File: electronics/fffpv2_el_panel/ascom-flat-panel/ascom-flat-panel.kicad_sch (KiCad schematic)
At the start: 19 parts, among them J1 Servo, J2 Conn_01x02, Q1 IRLZ34N, Q2 IRLZ34N, U1 XIAO-SAMD21-DIP, U2 TLC272

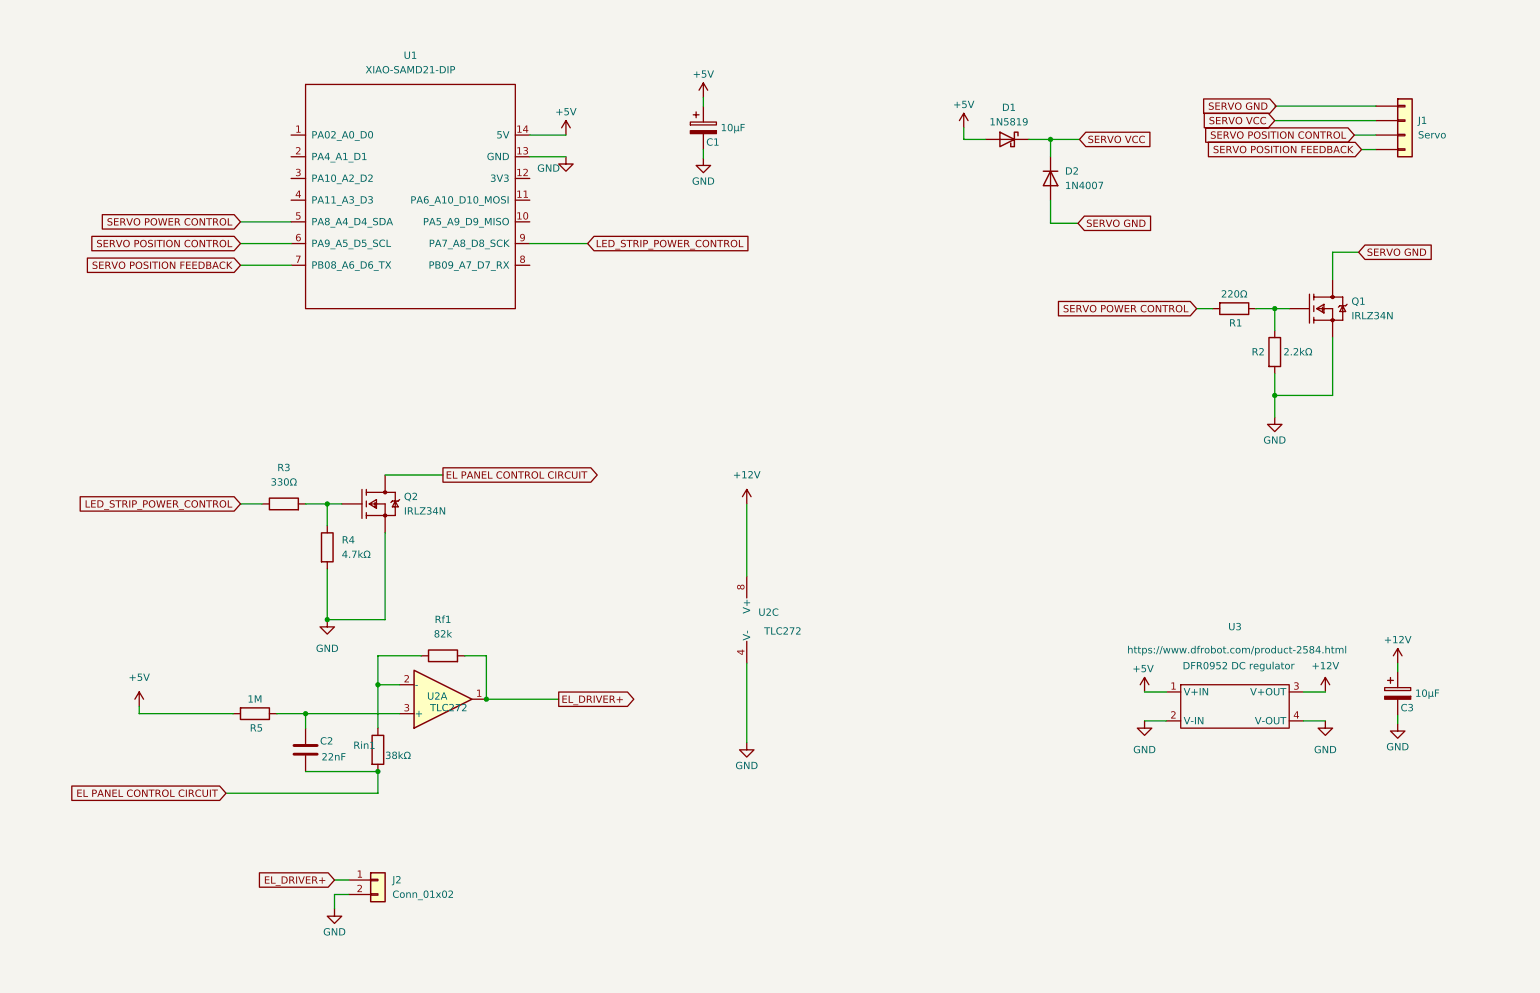
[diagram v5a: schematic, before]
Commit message: Flip connector for shorter traces and rearanged schematics
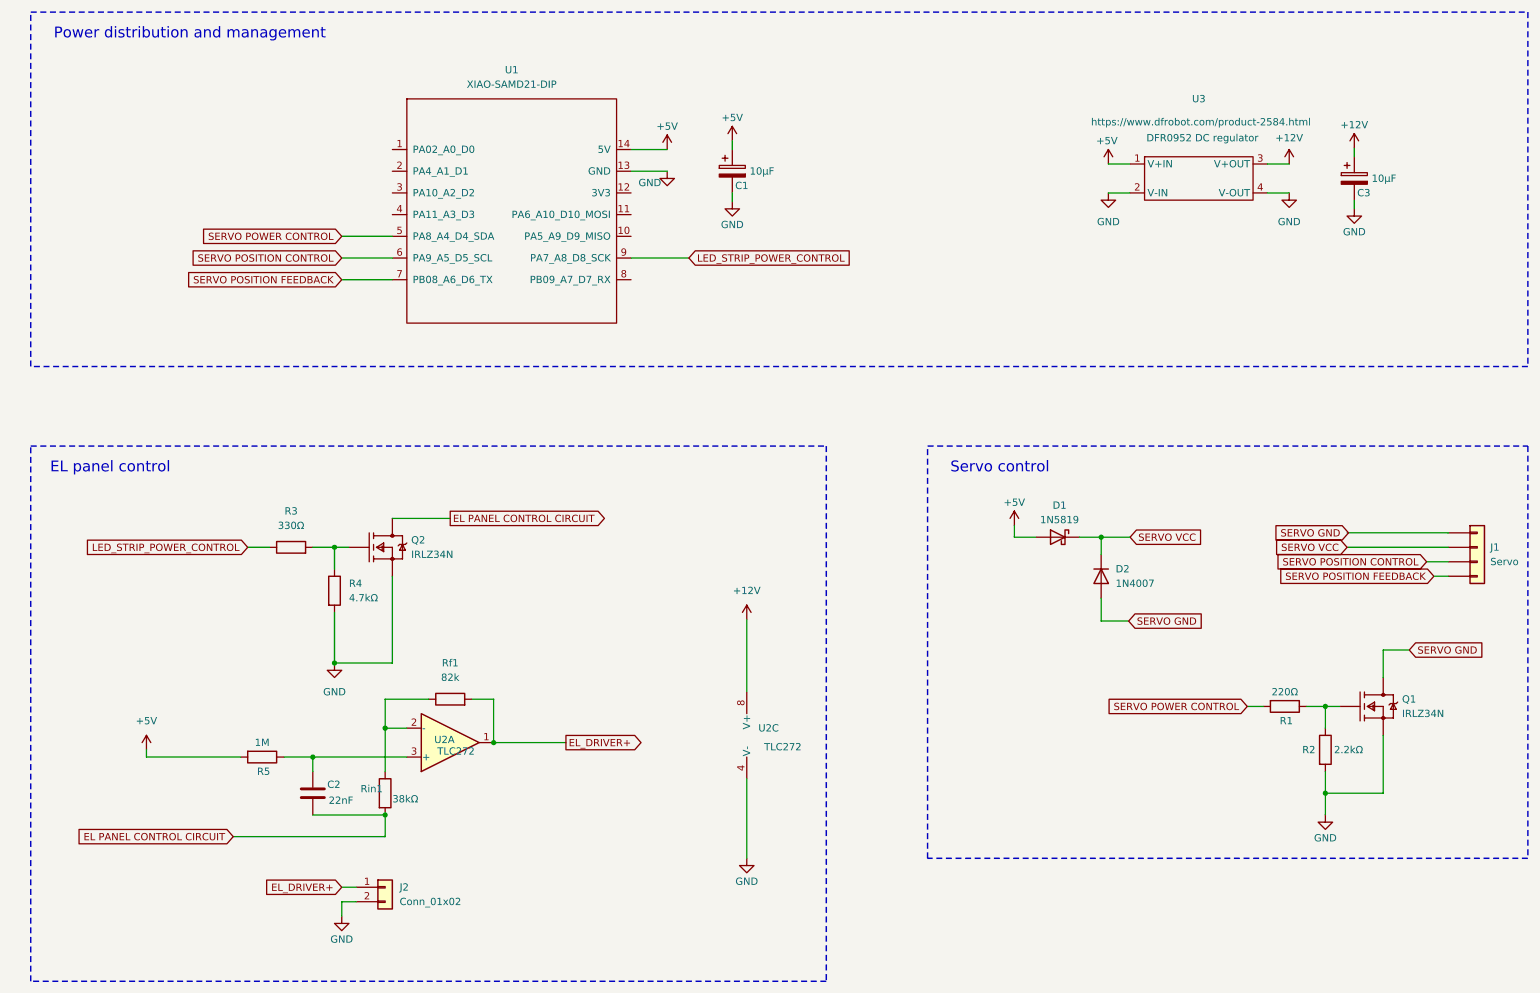
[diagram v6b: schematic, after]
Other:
- note added: "EL panel control"
- note added: "Power distribution and management"
- note added: "Servo control"
- moved on the sheet: C1, C2, C3, D1, D2, J1, J2, Q1, Q2, R1, R2, R3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

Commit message: Removed most warnings form ERC (schema) and DRC (pcb)
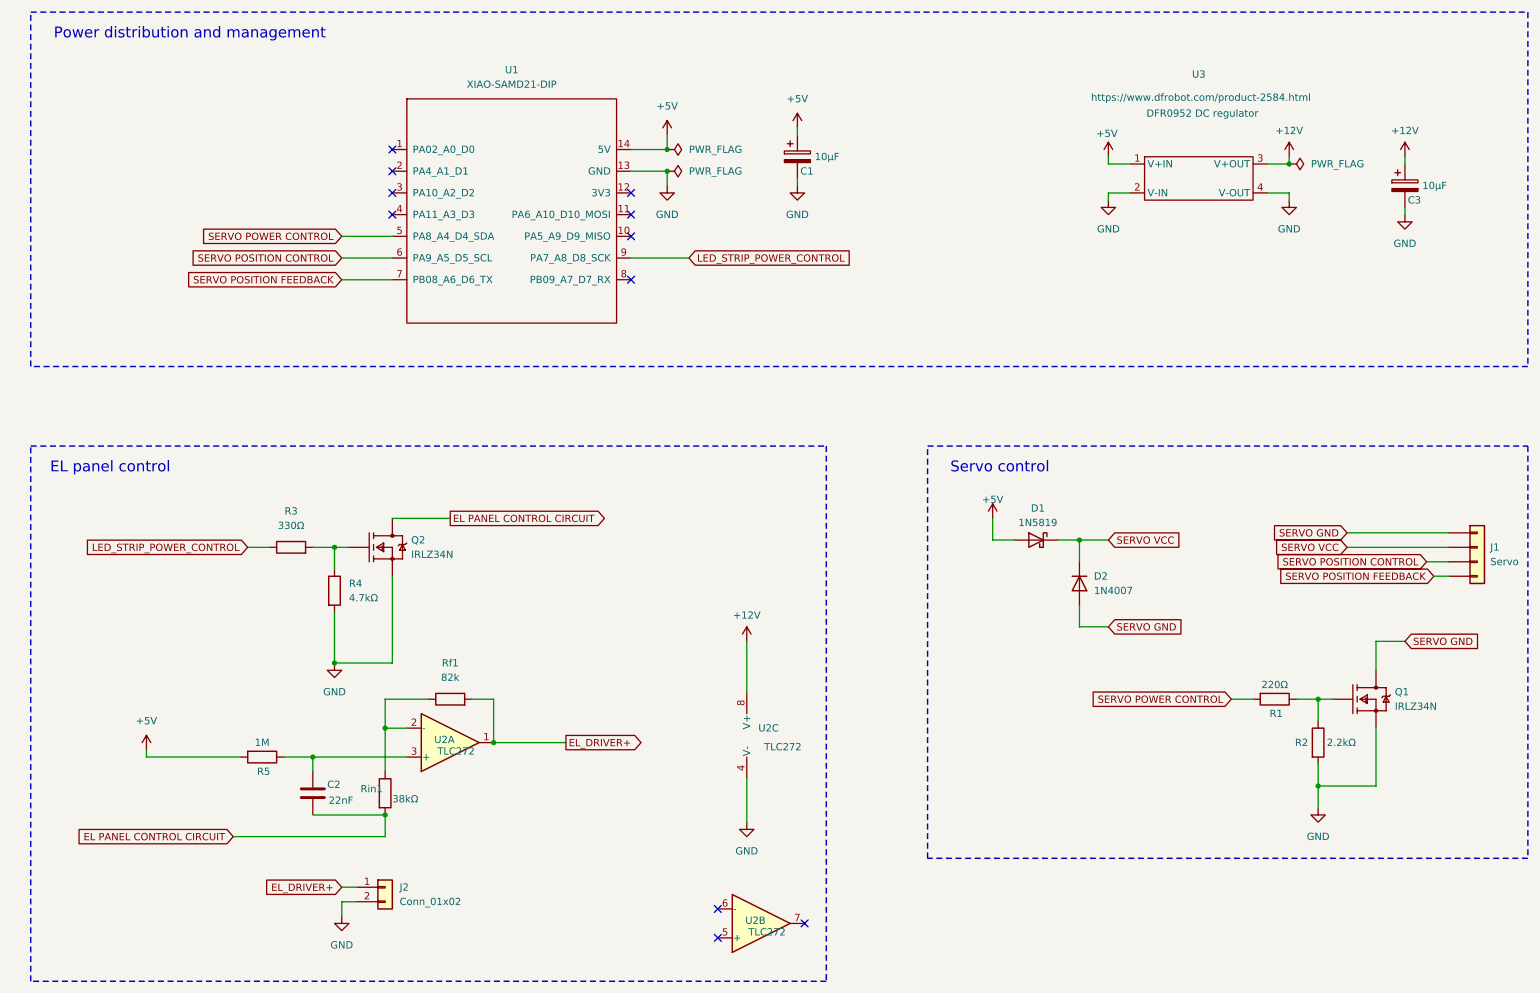
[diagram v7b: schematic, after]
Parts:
- added unit 2 of U2
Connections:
- no-connect marks 0 -> 11
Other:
- moved on the sheet: C1, C3, D1, D2, Q1, R1, R2

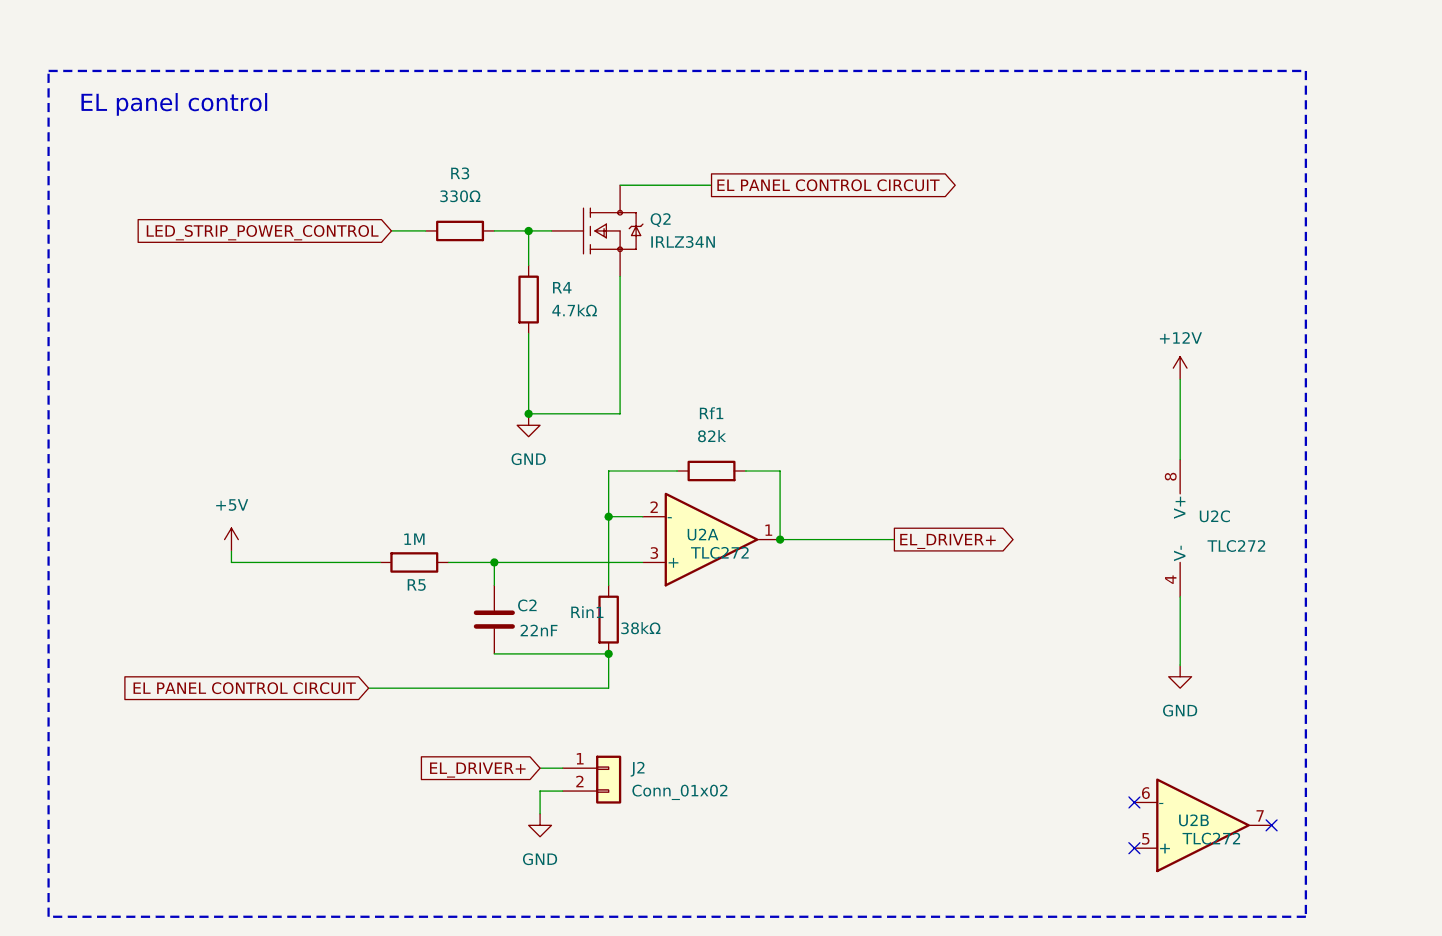
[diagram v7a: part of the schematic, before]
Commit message: Feedback from first breadboard prototype
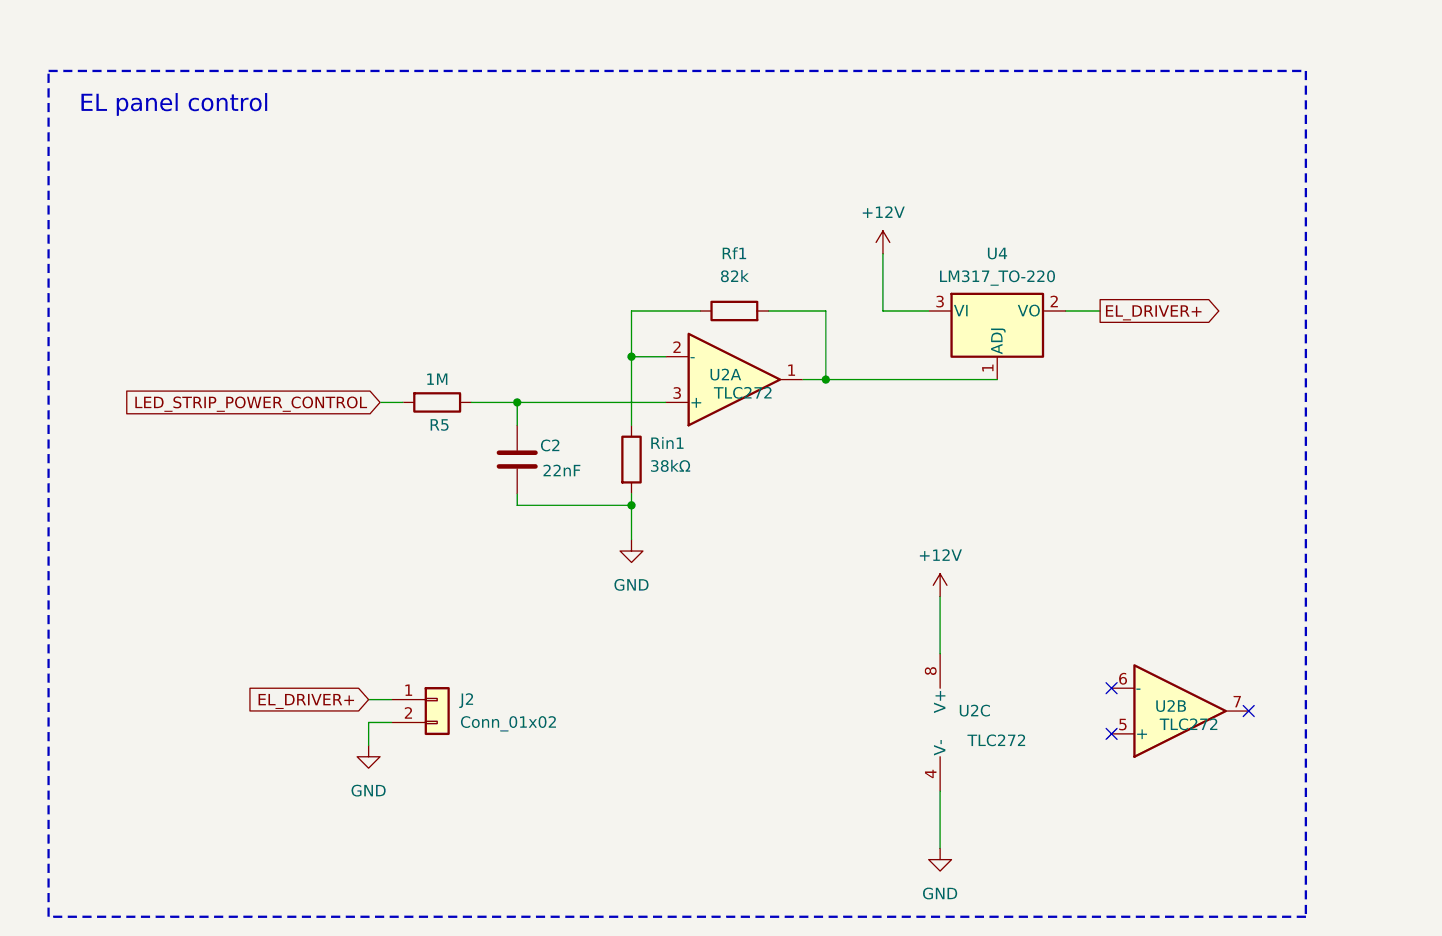
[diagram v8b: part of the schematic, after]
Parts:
- removed Q2: IRLZ34N, Package_TO_SOT_THT:TO-220-3_Vertical, symbol DarkSkyGeek_KiCad_Symbol_Library:FQP30N06L
- removed R3: 330Ω, Resistor_THT:R_Axial_DIN0207_L6.3mm_D2.5mm_P10.16mm_Horizontal, symbol Device:R
- removed R4: 4.7kΩ, Resistor_THT:R_Axial_DIN0207_L6.3mm_D2.5mm_P10.16mm_Horizontal, symbol Device:R
- added U4: LM317_TO-220, Package_TO_SOT_THT:TO-220-3_Vertical, symbol Regulator_Linear:LM317_TO-220
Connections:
- net EL PANEL CONTROL CIRCUIT is gone; now on net GND: C2.2, Rin1.2
- net +12V: now also U4.3 (VI)
- net +5V: no longer R5.2
- net EL_DRIVER+: now also U4.2 (VO); no longer Rf1.2, U2.1
- net LED_STRIP_POWER_CONTROL: now also R5.2
- new net: Rf1.2, U2.1, U4.1 (ADJ)
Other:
- moved on the sheet: C2, J2, R5, Rf1, Rin1, U2A, U2B, U2C
